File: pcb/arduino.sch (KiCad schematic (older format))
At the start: 57 parts, among them J1 Conn_Coaxial_Power, SW1 SW_DIP_x08, SW2 SW_DIP_x08, U1 ATMEGA328-PU

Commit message: Reworked the circuit from scratch.
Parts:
- removed SW1, SW2: SW_DIP_x08, Buttons_Switches_THT:SW_DIP_x8_W7.62mm_Slide, symbol SW_DIP_x08
- added C1: 100nF, Capacitors_THT:C_Disc_D3.0mm_W1.6mm_P2.50mm, symbol C
- added C2, C3: 22pF, Capacitors_THT:C_Disc_D3.0mm_W1.6mm_P2.50mm, symbol C
- added D10, MISO1, MOSI1, RXD1, SCK1, SCL1, SDA1, TXD1: DATA, Pin_Headers:Pin_Header_Straight_1x03_Pitch2.54mm, symbol DATA
- added FT1: FTDI, Pin_Headers:Pin_Header_Straight_1x06_Pitch2.54mm, symbol FTDI
- added H1, H3: Headers8L, Pin_Headers:Pin_Header_Straight_1x08_Pitch2.54mm, symbol Headers8L
- added H2, H4: Headers8, Pin_Headers:Pin_Header_Straight_1x08_Pitch2.54mm, symbol Headers8
- added LED1: FTDI, LEDs:LED_D3.0mm, symbol LED
- added LED2: VCC, LEDs:LED_D3.0mm, symbol LED
- added PR3, PR4: R, Resistors_THT:R_Axial_DIN0204_L3.6mm_D1.6mm_P5.08mm_Horizontal, symbol R
- added R1: 10K, Resistors_THT:R_Axial_DIN0204_L3.6mm_D1.6mm_P5.08mm_Horizontal, symbol R
- added RESET1: SW_Push, Buttons_Switches_THT:SW_PUSH_6mm, symbol SW_Push
- added SW1: SW_SPDT, Buttons_Switches_THT:SW_CuK_JS202011CQN_DPDT_Straight, symbol SW_SPDT
- added U2: L7805, Power_Integrations:TO-220, symbol L7805
- added Y1: 16MHz, Crystals:Resonator-2pin_w6.0mm_h3.0mm, symbol Crystal
- D2, D3, D4, D5, D6, D7, D8, D9: footprint LEDs:LED_D3.0mm -> LEDs:LED_PLCC_2835
- LED3: renamed from DP2; value LED -> BRD
- LED4: renamed from DP1; value LED -> VIN
- NANO1: footprint Arduino:Arduino_Nano_Socket -> Arduino:Arduino_Nano
- XA1: value Arduino_Mini_03_Socket -> Arduino_ProMini; footprint Arduino:Arduino_Mini_Socket -> Arduino:Arduino_ProMini
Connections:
- net Reset is gone; now on net RESET: U1.1 ((PCINT14/~RESET~)PC6)
- net A0: now also H2.1 (H1)
- net A1: now also H2.2 (H2)
- net A2: now also H2.3 (H3)
- net A3: now also H2.4 (H4)
- net A4: now also H2.5 (H5), SDA1.3 (DATA)
- net A5: now also I2C1.3 (SCK), I2C2.3 (SCK), I2C3.3 (SCK), I2C4.3 (SCK), H2.6 (H6), SCL1.3 (DATA)
- net A6: now also H2.7 (H7)
- net A7: now also H2.8 (H8)
- net AVCC: now also C1.1
- net D0: now also FT1.5 (RXI), RXD1.3 (DATA)
- net D1: now also FT1.4 (TXO), TXD1.3 (DATA)
- net D10: now also D10.3 (DATA)
- net D11: now also MOSI1.3 (DATA)
- net D12: now also MISO1.3 (DATA)
- net D13: now also SCK1.3 (DATA); no longer I2C1.3 (SCK), I2C2.3 (SCK), I2C3.3 (SCK), I2C4.3 (SCK)
- net Earth: now also C1.2, C2.2, C3.1, D10.1 (GND), FT1.1 (GND), FT1.2 (CTS), LED1.1 (K), LED2.1 (K), MISO1.1 (GND), MOSI1.1 (GND), RESET1.2, RXD1.1 (GND), SCK1.1 (GND), SCL1.1 (GND), SDA1.1 (GND), TXD1.1 (GND), U2.2 (GND); no longer LED4.1 (K), RV7.3
- net VCC: now also D10.2 (VCC), MISO1.2 (VCC), MOSI1.2 (VCC), PR4.1, R1.2, RXD1.2 (VCC), SCK1.2 (VCC), SCL1.2 (VCC), SDA1.2 (VCC), SW1.2 (B), TXD1.2 (VCC); no longer PR2.1
- net VIN: now also U2.1 (IN)
- net at R2.1: now also H3.1 (H1)
- net at R3.1: now also H3.2 (H2)
- net at R4.1: now also H3.3 (H3)
- net at R5.1: now also H3.4 (H4)
- net at R6.1: now also H3.5 (H5)
- net at R7.1: now also H3.6 (H6)
- net at R8.1: now also H3.7 (H7)
- net at R9.1: now also H3.8 (H8)
- net at D8.1 (K): now also H4.7 (H7)
- net at D7.1 (K): now also H4.6 (H6)
- net at D6.1 (K): now also H4.5 (H5)
- net at D5.1 (K): now also H4.4 (H4)
- net at D4.1 (K): now also H4.3 (H3)
- net at D3.1 (K): now also H4.2 (H2)
- net at D2.1 (K): now also H4.1 (H1)
- net at D9.1 (K): now also H4.8 (H8)
- net at RV0.2: now also H1.1 (H1)
- net at RV1.2: now also H1.2 (H2)
- net at RV2.2: now also H1.3 (H3)
- net at RV3.2: now also H1.4 (H4)
- net at RV4.2: now also H1.5 (H5)
- net at RV5.2: now also H1.6 (H6)
- net at RV6.2: now also H1.7 (H7)
- net at RV7.2: now also H1.8 (H8)
- net at U1.10 ((PCINT7/XTAL2/TOSC2)PB7): now also C3.2, Y1.1
- net at U1.9 ((PCINT6/XTAL1/TOSC1)PB6): now also C2.1, Y1.2
- net RESET: now reaches XA1.L2 (IO7)
- net RESET: now also FT1.6 (DTR), R1.1, RESET1.1
- net at LED3.2 (A): now also PR2.1; no longer PR2.2
- new net: PR2.2, SW1.3 (C), U2.3 (OUT)
- new net: FT1.3 (VCC), PR3.1, SW1.1 (A)
- new net: LED1.2 (A), PR3.2
- new net: LED2.2 (A), PR4.2
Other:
- moved on the sheet: A0, A1, A2, A3, A4, A5, A6, A7, D2, D3, D4, D5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

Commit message: Tidy up - Note, there is a problem with VIN.
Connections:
- net RESET: now also NANO1.RST2 (RESET)
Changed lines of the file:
@@
 Text Label 7600 5950 2    60   ~ 0
 VCC
+Text Label 6700 2850 0    60   ~ 0
+RESET
 $EndSCHEMATC

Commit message: More tweaking of the layout.
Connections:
- net RESET: now also XA1.RST2 (RESET); no longer XA1.L2 (IO7)
- net VIN: no longer NANO1.VIN, XA1.VIN
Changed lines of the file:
@@
 Text Label 4100 2750 2    60   ~ 0
 3V3
-Text Label 4100 2950 2    60   ~ 0
-VIN
 Text Label 4100 2850 2    60   ~ 0
 VCC
@@
 Text Label 4100 5150 2    60   ~ 0
 VCC
-Text Label 4100 5350 2    60   ~ 0
-VIN
 $Comp
 L Conn_Coaxial_Power J1
@@
 Text Label 2200 5750 3    60   ~ 0
 GND
-Text Label 6700 4750 0    60   ~ 0
+Text Label 6700 5400 0    60   ~ 0
 RESET
 Text Label 7600 5950 2    60   ~ 0

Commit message: Replaced surface mount LEDs with rectangular through hole. Removed PRO-Mini FTDI Header pins from the footprint.
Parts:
- D2, D3, D4, D5, D6, D7, D8, D9: footprint LEDs:LED_PLCC_2835 -> LEDs:LED_Rectangular_W5.0mm_H2.0mm
- XA1: footprint Arduino:Arduino_ProMini -> Arduino:Arduino_ProMini_NoFTDI
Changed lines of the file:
@@
 F 0 "D2" H 8700 1300 50  0000 C CNN
 F 1 "LED" H 8350 1300 50  0000 C CNN
-F 2 "LEDs:LED_PLCC_2835" H 8500 1250 50  0001 C CNN
+F 2 "LEDs:LED_Rectangular_W5.0mm_H2.0mm" H 8500 1250 50  0001 C CNN
 F 3 "" H 8500 1250 50  0001 C CNN
 	1    8500 1250
@@
 F 0 "D3" H 8700 1400 50  0000 C CNN
 F 1 "LED" H 8350 1400 50  0000 C CNN
-F 2 "LEDs:LED_PLCC_2835" H 8500 1350 50  0001 C CNN
+F 2 "LEDs:LED_Rectangular_W5.0mm_H2.0mm" H 8500 1350 50  0001 C CNN
 F 3 "" H 8500 1350 50  0001 C CNN
 	1    8500 1350
@@
 F 0 "D4" H 8700 1500 50  0000 C CNN
 F 1 "LED" H 8350 1500 50  0000 C CNN
-F 2 "LEDs:LED_PLCC_2835" H 8500 1450 50  0001 C CNN
+F 2 "LEDs:LED_Rectangular_W5.0mm_H2.0mm" H 8500 1450 50  0001 C CNN
 F 3 "" H 8500 1450 50  0001 C CNN
 	1    8500 1450
@@
 F 0 "D5" H 8700 1600 50  0000 C CNN
 F 1 "LED" H 8350 1600 50  0000 C CNN
-F 2 "LEDs:LED_PLCC_2835" H 8500 1550 50  0001 C CNN
+F 2 "LEDs:LED_Rectangular_W5.0mm_H2.0mm" H 8500 1550 50  0001 C CNN
 F 3 "" H 8500 1550 50  0001 C CNN
 	1    8500 1550
@@
 F 0 "D6" H 8700 1700 50  0000 C CNN
 F 1 "LED" H 8350 1700 50  0000 C CNN
-F 2 "LEDs:LED_PLCC_2835" H 8500 1650 50  0001 C CNN
+F 2 "LEDs:LED_Rectangular_W5.0mm_H2.0mm" H 8500 1650 50  0001 C CNN
 F 3 "" H 8500 1650 50  0001 C CNN
 	1    8500 1650
@@
 F 0 "D7" H 8700 1800 50  0000 C CNN
 F 1 "LED" H 8350 1800 50  0000 C CNN
-F 2 "LEDs:LED_PLCC_2835" H 8500 1750 50  0001 C CNN
+F 2 "LEDs:LED_Rectangular_W5.0mm_H2.0mm" H 8500 1750 50  0001 C CNN
 F 3 "" H 8500 1750 50  0001 C CNN
 	1    8500 1750
@@
 F 0 "D8" H 8700 1900 50  0000 C CNN
 F 1 "LED" H 8350 1900 50  0000 C CNN
-F 2 "LEDs:LED_PLCC_2835" H 8500 1850 50  0001 C CNN
+F 2 "LEDs:LED_Rectangular_W5.0mm_H2.0mm" H 8500 1850 50  0001 C CNN
 F 3 "" H 8500 1850 50  0001 C CNN
 	1    8500 1850
@@
 F 0 "D9" H 8700 2000 50  0000 C CNN
 F 1 "LED" H 8350 2000 50  0000 C CNN
-F 2 "LEDs:LED_PLCC_2835" H 8500 1950 50  0001 C CNN
+F 2 "LEDs:LED_Rectangular_W5.0mm_H2.0mm" H 8500 1950 50  0001 C CNN
 F 3 "" H 8500 1950 50  0001 C CNN
 	1    8500 1950
@@
 F 0 "XA1" V 5500 4450 60  0000 C CNN
 F 1 "Arduino_ProMini" V 5300 4450 60  0000 C CNN
-F 2 "Arduino:Arduino_ProMini" H 7200 8200 60  0001 C CNN
+F 2 "Arduino:Arduino_ProMini_NoFTDI" H 7200 8200 60  0001 C CNN
 F 3 "" H 7200 8200 60  0001 C CNN
 	1    5400 4450

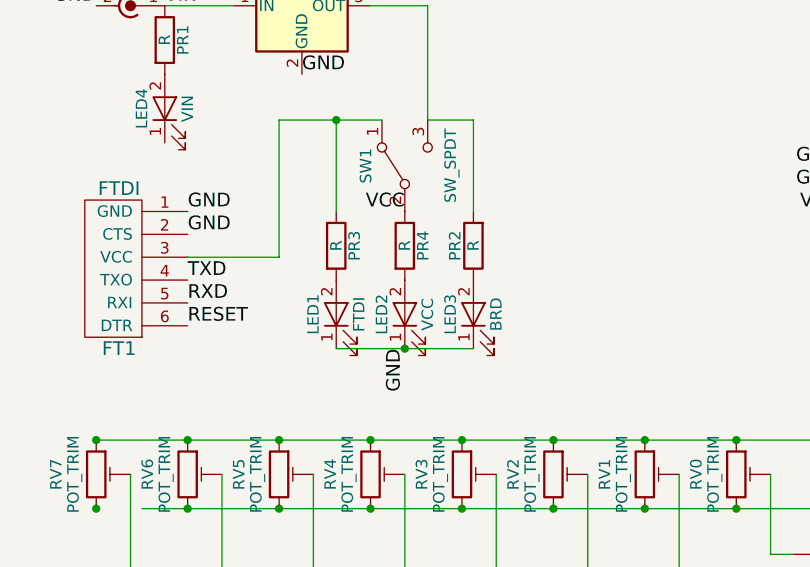
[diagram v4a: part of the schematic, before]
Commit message: Incfreased resistor size. Improved the ProMini footprint. Removed the VCC LED.
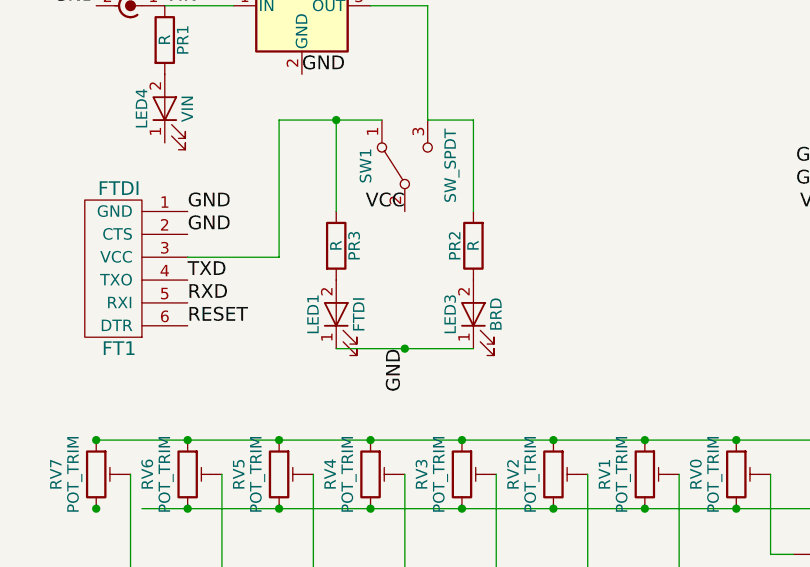
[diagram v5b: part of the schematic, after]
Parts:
- removed LED2: VCC, LEDs:LED_D3.0mm, symbol LED
- removed PR4: R, Resistors_THT:R_Axial_DIN0204_L3.6mm_D1.6mm_P5.08mm_Horizontal, symbol R
- PR1, PR2, PR3, R1, R2, R3, R4, R5, R6, R7, R8, R9: footprint Resistors_THT:R_Axial_DIN0204_L3.6mm_D1.6mm_P5.08mm_Horizontal -> Resistors_THT:R_Axial_DIN0204_L3.6mm_D1.6mm_P7.62mm_Horizontal
- XA1: footprint Arduino:Arduino_ProMini_NoFTDI -> Arduino:Arduino_ProMini_NoICSP
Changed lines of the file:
@@
 F 0 "R2" V 7400 1000 50  0000 C CNN
 F 1 "R" V 7400 1250 50  0000 C CNN
-F 2 "Resistors_THT:R_Axial_DIN0204_L3.6mm_D1.6mm_P5.08mm_Horizontal" V 7330 1250 50  0001 C CNN
+F 2 "Resistors_THT:R_Axial_DIN0204_L3.6mm_D1.6mm_P7.62mm_Horizontal" V 7330 1250 50  0001 C CNN
 F 3 "" H 7400 1250 50  0001 C CNN
 	1    7400 1250
@@
 F 0 "R3" V 7400 1100 50  0000 C CNN
 F 1 "R" V 7400 1350 50  0000 C CNN
-F 2 "Resistors_THT:R_Axial_DIN0204_L3.6mm_D1.6mm_P5.08mm_Horizontal" V 7330 1350 50  0001 C CNN
+F 2 "Resistors_THT:R_Axial_DIN0204_L3.6mm_D1.6mm_P7.62mm_Horizontal" V 7330 1350 50  0001 C CNN
 F 3 "" H 7400 1350 50  0001 C CNN
 	1    7400 1350
@@
 F 0 "R4" V 7400 1200 50  0000 C CNN
 F 1 "R" V 7400 1450 50  0000 C CNN
-F 2 "Resistors_THT:R_Axial_DIN0204_L3.6mm_D1.6mm_P5.08mm_Horizontal" V 7330 1450 50  0001 C CNN
+F 2 "Resistors_THT:R_Axial_DIN0204_L3.6mm_D1.6mm_P7.62mm_Horizontal" V 7330 1450 50  0001 C CNN
 F 3 "" H 7400 1450 50  0001 C CNN
 	1    7400 1450
@@
 F 0 "R5" V 7400 1300 50  0000 C CNN
 F 1 "R" V 7400 1550 50  0000 C CNN
-F 2 "Resistors_THT:R_Axial_DIN0204_L3.6mm_D1.6mm_P5.08mm_Horizontal" V 7330 1550 50  0001 C CNN
+F 2 "Resistors_THT:R_Axial_DIN0204_L3.6mm_D1.6mm_P7.62mm_Horizontal" V 7330 1550 50  0001 C CNN
 F 3 "" H 7400 1550 50  0001 C CNN
 	1    7400 1550
@@
 F 0 "R6" V 7400 1400 50  0000 C CNN
 F 1 "R" V 7400 1650 50  0000 C CNN
-F 2 "Resistors_THT:R_Axial_DIN0204_L3.6mm_D1.6mm_P5.08mm_Horizontal" V 7330 1650 50  0001 C CNN
+F 2 "Resistors_THT:R_Axial_DIN0204_L3.6mm_D1.6mm_P7.62mm_Horizontal" V 7330 1650 50  0001 C CNN
 F 3 "" H 7400 1650 50  0001 C CNN
 	1    7400 1650
@@
 F 0 "R7" V 7400 1500 50  0000 C CNN
 F 1 "R" V 7400 1750 50  0000 C CNN
-F 2 "Resistors_THT:R_Axial_DIN0204_L3.6mm_D1.6mm_P5.08mm_Horizontal" V 7330 1750 50  0001 C CNN
+F 2 "Resistors_THT:R_Axial_DIN0204_L3.6mm_D1.6mm_P7.62mm_Horizontal" V 7330 1750 50  0001 C CNN
 F 3 "" H 7400 1750 50  0001 C CNN
 	1    7400 1750
@@
 F 0 "R8" V 7400 1600 50  0000 C CNN
 F 1 "R" V 7400 1850 50  0000 C CNN
-F 2 "Resistors_THT:R_Axial_DIN0204_L3.6mm_D1.6mm_P5.08mm_Horizontal" V 7330 1850 50  0001 C CNN
+F 2 "Resistors_THT:R_Axial_DIN0204_L3.6mm_D1.6mm_P7.62mm_Horizontal" V 7330 1850 50  0001 C CNN
 F 3 "" H 7400 1850 50  0001 C CNN
 	1    7400 1850
@@
 F 0 "R9" V 7400 1700 50  0000 C CNN
 F 1 "R" V 7400 1950 50  0000 C CNN
-F 2 "Resistors_THT:R_Axial_DIN0204_L3.6mm_D1.6mm_P5.08mm_Horizontal" V 7330 1950 50  0001 C CNN
+F 2 "Resistors_THT:R_Axial_DIN0204_L3.6mm_D1.6mm_P7.62mm_Horizontal" V 7330 1950 50  0001 C CNN
 F 3 "" H 7400 1950 50  0001 C CNN
 	1    7400 1950
@@
 F 0 "XA1" V 5500 4450 60  0000 C CNN
 F 1 "Arduino_ProMini" V 5300 4450 60  0000 C CNN
-F 2 "Arduino:Arduino_ProMini_NoFTDI" H 7200 8200 60  0001 C CNN
+F 2 "Arduino:Arduino_ProMini_NoICSP" H 7200 8200 60  0001 C CNN
 F 3 "" H 7200 8200 60  0001 C CNN
 	1    5400 4450
@@
 F 0 "PR1" V 1230 4400 50  0000 C CNN
 F 1 "R" V 1150 4400 50  0000 C CNN
-F 2 "Resistors_THT:R_Axial_DIN0204_L3.6mm_D1.6mm_P5.08mm_Horizontal" V 1080 4400 50  0001 C CNN
+F 2 "Resistors_THT:R_Axial_DIN0204_L3.6mm_D1.6mm_P7.62mm_Horizontal" V 1080 4400 50  0001 C CNN
 F 3 "" H 1150 4400 50  0001 C CNN
 	1    1150 4400
@@
 F 0 "PR2" V 2580 5300 50  0000 C CNN
 F 1 "R" V 2500 5300 50  0000 C CNN
-F 2 "Resistors_THT:R_Axial_DIN0204_L3.6mm_D1.6mm_P5.08mm_Horizontal" V 2430 5300 50  0001 C CNN
+F 2 "Resistors_THT:R_Axial_DIN0204_L3.6mm_D1.6mm_P7.62mm_Horizontal" V 2430 5300 50  0001 C CNN
 F 3 "" H 2500 5300 50  0001 C CNN
 	1    2500 5300
@@
 F 0 "R1" V 3430 2350 50  0000 C CNN
 F 1 "10K" V 3350 2350 50  0000 C CNN
-F 2 "Resistors_THT:R_Axial_DIN0204_L3.6mm_D1.6mm_P5.08mm_Horizontal" V 3280 2350 50  0001 C CNN
+F 2 "Resistors_THT:R_Axial_DIN0204_L3.6mm_D1.6mm_P7.62mm_Horizontal" V 3280 2350 50  0001 C CNN
 F 3 "" H 3350 2350 50  0001 C CNN
 	1    3350 2350
@@
 F 0 "PR3" V 1980 5300 50  0000 C CNN
 F 1 "R" V 1900 5300 50  0000 C CNN
-F 2 "Resistors_THT:R_Axial_DIN0204_L3.6mm_D1.6mm_P5.08mm_Horizontal" V 1830 5300 50  0001 C CNN
+F 2 "Resistors_THT:R_Axial_DIN0204_L3.6mm_D1.6mm_P7.62mm_Horizontal" V 1830 5300 50  0001 C CNN
 F 3 "" H 1900 5300 50  0001 C CNN
 	1    1900 5300
@@
 $EndComp
 $Comp
-L R PR4
-U 1 1 5AC2175E
-P 2200 5300
-F 0 "PR4" V 2280 5300 50  0000 C CNN
-F 1 "R" V 2200 5300 50  0000 C CNN
-F 2 "Resistors_THT:R_Axial_DIN0204_L3.6mm_D1.6mm_P5.08mm_Horizontal" V 2130 5300 50  0001 C CNN
-F 3 "" H 2200 5300 50  0001 C CNN
-	1    2200 5300
-	1    0    0    -1
-$EndComp
-$Comp
-L LED LED2
-U 1 1 5AC22481
-P 2200 5600
-F 0 "LED2" H 2200 5700 50  0000 C CNN
-F 1 "VCC" H 2200 5500 50  0000 C CNN
-F 2 "LEDs:LED_D3.0mm" H 2200 5600 50  0001 C CNN
-F 3 "" H 2200 5600 50  0001 C CNN
-	1    2200 5600
-	0    -1   -1   0
-$EndComp
-$Comp
